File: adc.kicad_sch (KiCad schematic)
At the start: 24 parts, among them U1 ADA4945-1, U2 LTC2387-18

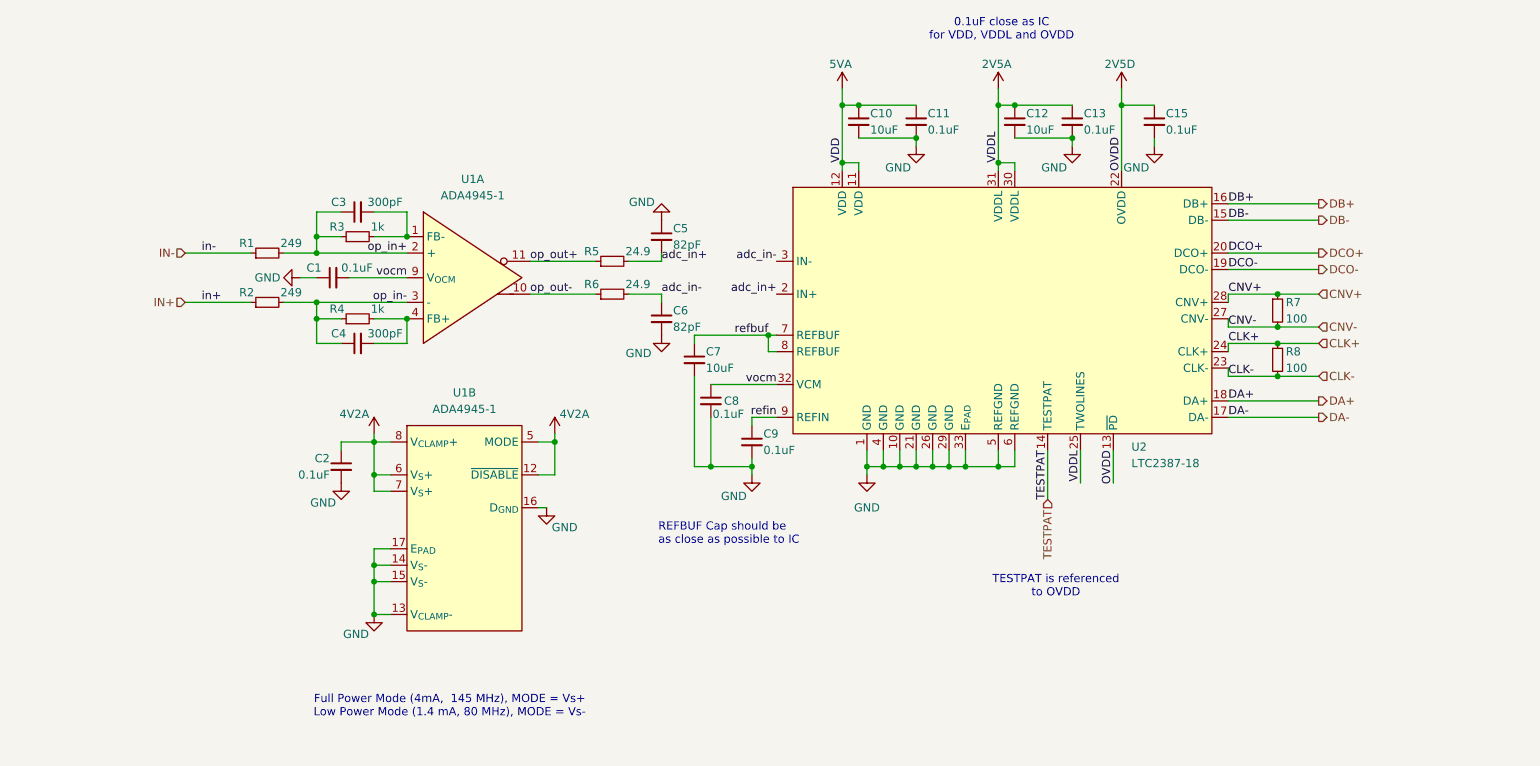
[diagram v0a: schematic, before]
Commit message: add instrumentation amplifier front-end
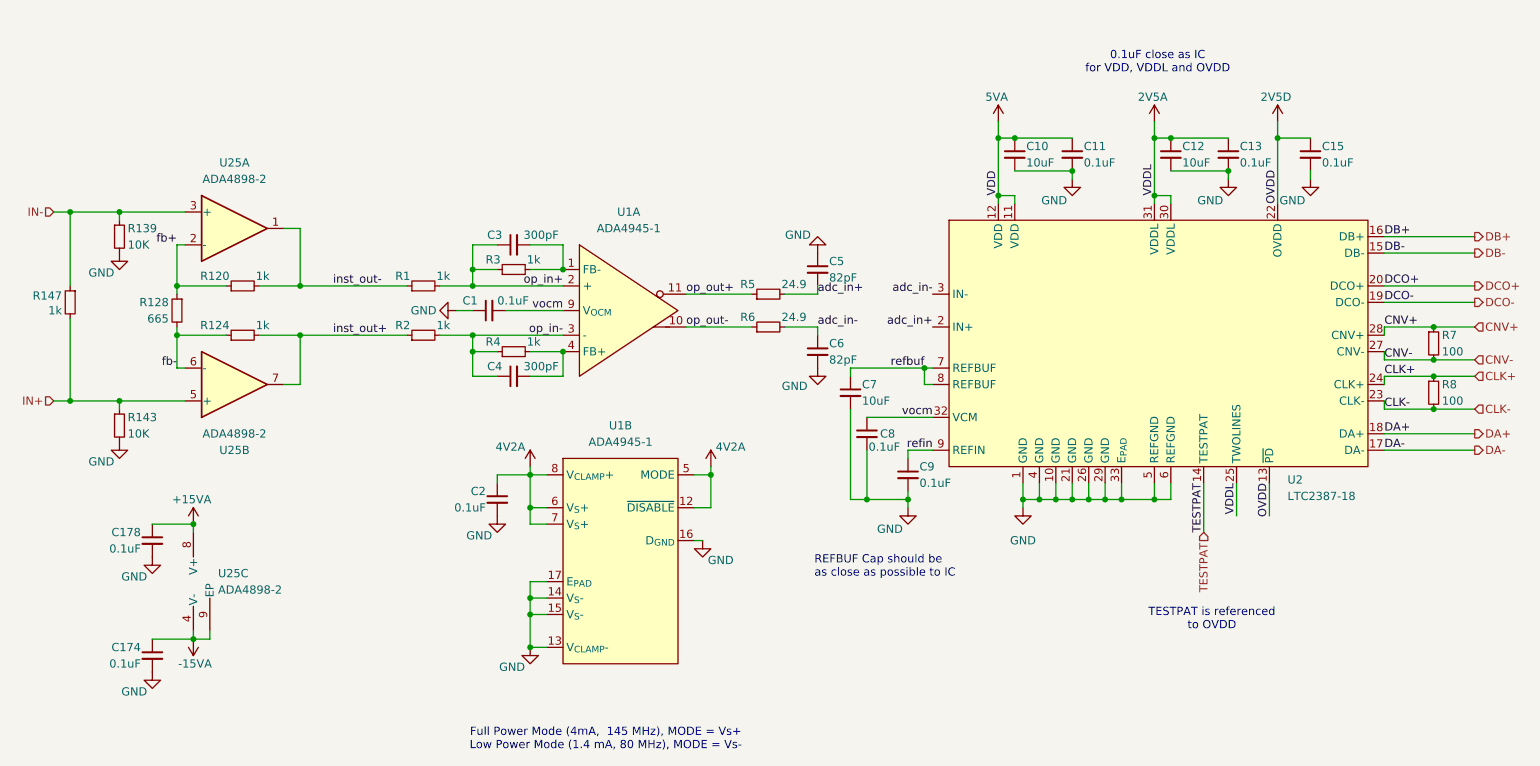
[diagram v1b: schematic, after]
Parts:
- added C174, C178: 0.1uF, Capacitor_SMD:C_0402_1005Metric, symbol Device:C_Small
- added R120, R124, R147: 1k, Resistor_SMD:R_0603_1608Metric, symbol Device:R_Small
- added R128: 665, Resistor_SMD:R_0603_1608Metric, symbol Device:R_Small
- added R139, R143: 10K, Resistor_SMD:R_0603_1608Metric, symbol Device:R_Small
- added U25: ADA4898-2, Package_SO:SOIC-8-1EP_3.9x4.9mm_P1.27mm_EP2.41x3.81mm, symbol Amplifier_Operational:ADA4898-2
- R1, R2: value 249 -> 1k; MPN ERJ-PB3B2490V -> ERA-3AEB102V
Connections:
- net GND: now also C174.2, C178.2, R139.2, R143.2
- net IN+: now also R143.1, R147.2, U25.5 (+); no longer R2.1
- net IN-: now also R139.1, R147.1, U25.3 (+); no longer R1.1
- new net +15VA: C178.1, U25.8 (V+)
- new net -15VA: C174.1, U25.4 (V-), U25.9 (EP)
- new net fb+: R120.1, R128.1, U25.2 (-)
- new net fb-: R124.1, R128.2, U25.6 (-)
- new net inst_out+: R124.2, R2.1, U25.7
- new net inst_out-: R1.1, R120.2, U25.1
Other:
- moved on the sheet: C1, C10, C11, C12, C13, C15, C2, C3, C4, C5, C6, C7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
